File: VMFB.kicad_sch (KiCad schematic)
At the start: 109 parts, among them J1 Barrel_Jack_Switch, J10 Conn_01x03_Pin, J11 Conn_01x08_Pin, J12 Conn_01x04_Pin, J13 Conn_01x04_Pin, J14 Conn_01x04_Pin, J2 USB_B, J3 Screw_Terminal_01x02, J4 Screw_Terminal_01x03, J5 Conn_01x03_Pin, J6 Conn_01x04_Pin, J7 Conn_01x04_Pin, J8 Conn_01x04_Pin, J9 Conn_01x02_Pin, Q1 BC547, Q2 BC547, Q3 BC547, Q4 BD139, Q5 TIP41C, Q6 BC547, U1 LM358, U2 NE555P, U3 NE555P, U4 NE555P, U5 NE555P

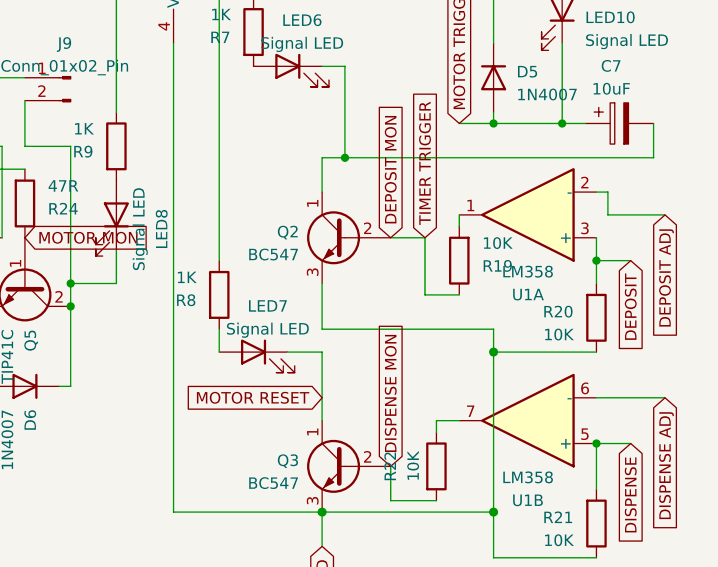
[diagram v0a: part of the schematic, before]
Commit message: Added 1uf cap on the dispense transistor base to prevent triggering on power-up.
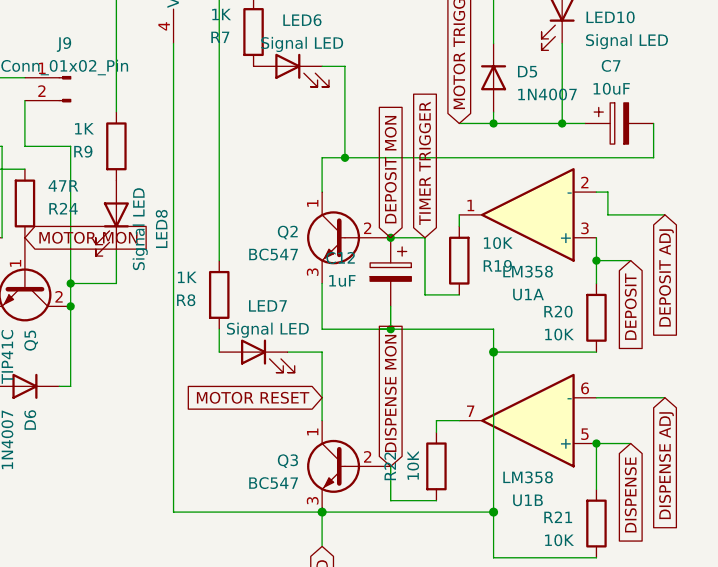
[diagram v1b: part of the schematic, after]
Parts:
- added C12: 1uF, Capacitor_THT:CP_Radial_D5.0mm_P2.00mm, symbol Device:C_Polarized
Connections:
- net DEPOSIT MON: now also C12.1
- net GND: now also C12.2
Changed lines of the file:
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@@
   (title_block
     (title "Vending Machine For Birds")
-    (date "2023-05-05")
-    (rev "A1.1")
+    (date "2023-06-23")
+    (rev "A1.2")
   )
   (junction (at 74.93 115.57) (diameter 0) (color 0 0 0 0)
@@
   (junction (at 57.15 95.25) (diameter 0) (color 221 119 0 1)
   )
+  (junction (at 251.46 54.61) (diameter 0) (color 0 0 0 0)
+  )
   (junction (at 110.49 27.94) (diameter 0) (color 194 0 0 1)
   )
@@
   )
   (junction (at 33.02 156.21) (diameter 1) (color 0 0 0 1)
+  )
+  (junction (at 251.46 64.77) (diameter 0) (color 0 0 0 0)
   )
   (junction (at 57.15 97.79) (diameter 1) (color 221 119 0 1)
@@
     (stroke (width 0) (type default) (color 153 12 207 1))
   )
+  (wire (pts (xy 251.46 64.77) (xy 262.89 64.77))
+    (stroke (width 0) (type default) (color 0 0 0 1))
+  )
   (wire (pts (xy 36.83 149.86) (xy 33.02 149.86))
     (stroke (width 0) (type default) (color 0 0 0 1))
@@
     (stroke (width 0) (type default))
   )
+  (wire (pts (xy 251.46 62.23) (xy 251.46 64.77))
+    (stroke (width 0) (type default))
+  )
   (wire (pts (xy 132.08 71.12) (xy 132.08 80.01))
     (stroke (width 0) (type default) (color 0 0 0 1))
@@
     (stroke (width 0) (type default))
   )
+  (wire (pts (xy 251.46 64.77) (xy 250.19 64.77))
+    (stroke (width 0) (type default))
+  )
   (wire (pts (xy 54.61 110.49) (xy 54.61 120.65))
     (stroke (width 0) (type default))
@@
     (stroke (width 0) (type default) (color 0 255 0 1))
   )
-  (wire (pts (xy 243.84 64.77) (xy 262.89 64.77))
+  (wire (pts (xy 243.84 64.77) (xy 251.46 64.77))
     (stroke (width 0) (type default) (color 0 0 0 1))
   )
@@
         )
       )
+    )
+  )
+  (symbol (lib_id "Device:C_Polarized") (at 251.46 58.42 0) (mirror y) (unit 1)
+    (in_bom yes) (on_board yes) (dnp no)
+    (property "Reference" "C12" (at 247.65 56.896 0)
+      (effects (font (size 1.27 1.27)) (justify left))
+    )
+    (property "Value" "1uF" (at 247.65 59.436 0)
+      (effects (font (size 1.27 1.27)) (justify left))
+    )
+    (property "Footprint" "Capacitor_THT:CP_Radial_D5.0mm_P2.00mm" (at 250.4948 62.23 0)
+      (effects (font (size 1.27 1.27)) hide)
+    )
+    (property "Datasheet" "~" (at 251.46 58.42 0)
+      (effects (font (size 1.27 1.27)) hide)
+    )
+    (pin "1")
+    (pin "2")
+    (instances
+      (project "VMFB"
+        (path "/840789ee-60d4-4003-8113-c1b030a45492"
+          (reference "C12") (unit 1)
+        )
+      )

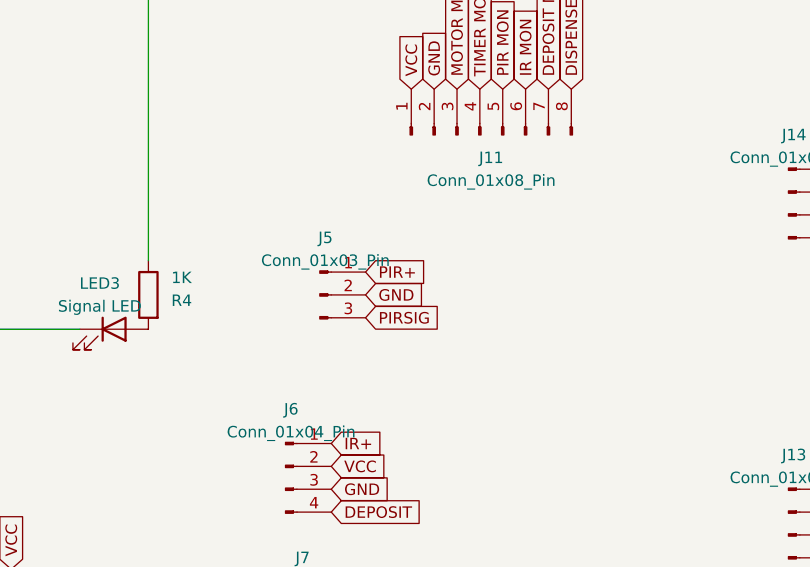
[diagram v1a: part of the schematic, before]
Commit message: Swapped PIR+ and GND to better accomodate common PIR pinouts.
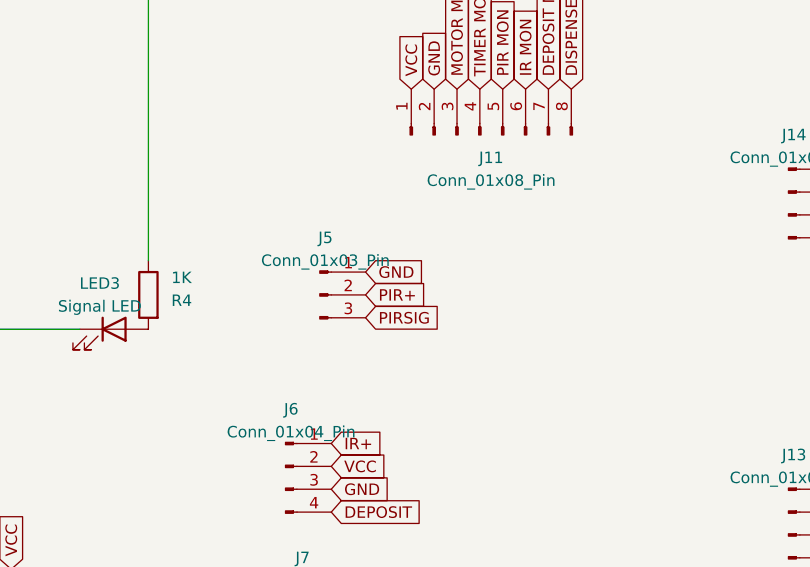
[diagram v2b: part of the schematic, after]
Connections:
- net GND: now also J5.1 (Pin_1); no longer J5.2 (Pin_2)
- net PIR+: now also J5.2 (Pin_2); no longer J5.1 (Pin_1)
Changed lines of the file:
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@@
     )
   )
-  (global_label "GND" (shape input) (at 149.86 123.19 0) (fields_autoplaced)
-    (effects (font (size 1.27 1.27)) (justify left))
-    (property "Intersheetrefs" "${INTERSHEET_REFS}" (at 156.6363 123.19 0) (show_name)
+  (global_label "GND" (shape input) (at 149.86 120.65 0) (fields_autoplaced)
+    (effects (font (size 1.27 1.27)) (justify left))
+    (property "Intersheetrefs" "${INTERSHEET_REFS}" (at 156.6363 120.65 0) (show_name)
       (effects (font (size 1.27 1.27)) (justify left) hide)
     )
@@
     )
   )
-  (global_label "PIR+" (shape input) (at 149.86 120.65 0) (fields_autoplaced)
-    (effects (font (size 1.27 1.27)) (justify left))
-    (property "Intersheetrefs" "${INTERSHEET_REFS}" (at 157.483 120.65 0) (show_name)
-      (effects (font (size 1.27 1.27)) (justify left) hide)
-    )
+  (global_label "PIR+" (shape input) (at 149.86 123.19 0) (fields_autoplaced)
+    (effects (font (size 1.27 1.27)) (justify left))
+    (property "Intersheetrefs" "${INTERSHEET_REFS}" (at 157.483 123.19 0) (show_name)
+      (effects (font (size 1.27 1.27)) (justify left) hide)
+    )

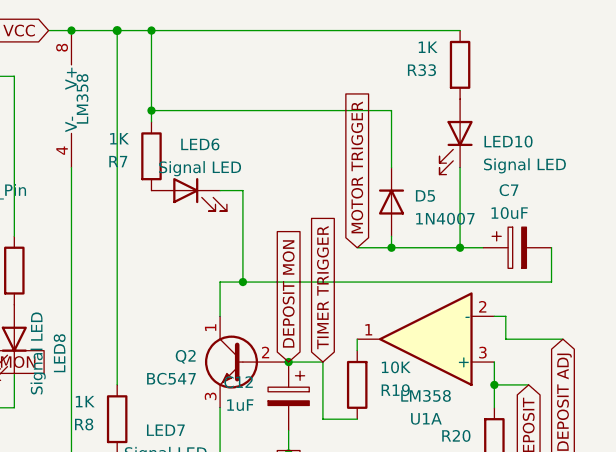
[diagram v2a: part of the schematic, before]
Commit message: Added 100K bleeder resistor across the pulse-shortening cap C7
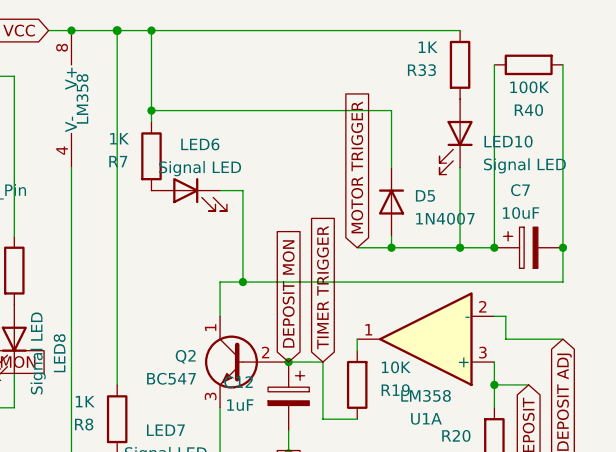
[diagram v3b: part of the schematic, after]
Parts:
- added R40: 100K, Resistor_THT:R_Axial_DIN0207_L6.3mm_D2.5mm_P2.54mm_Vertical, symbol Device:R
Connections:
- net MOTOR TRIGGER: now also R40.1
- net at C7.2, LED6.1 (K), Q2.1 (C): now also R40.2
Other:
- moved on the sheet: C7
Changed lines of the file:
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@@
   (junction (at 110.49 27.94) (diameter 0) (color 194 0 0 1)
   )
+  (junction (at 281.94 41.91) (diameter 0) (color 0 0 0 0)
+  )
   (junction (at 182.88 40.64) (diameter 1) (color 194 0 0 1)
   )
@@
   )
   (junction (at 69.85 130.81) (diameter 0) (color 0 0 0 1)
+  )
+  (junction (at 274.32 41.91) (diameter 0) (color 0 0 0 0)
   )
   (junction (at 262.89 85.09) (diameter 1) (color 0 0 0 1)
@@
     (stroke (width 0) (type default) (color 0 0 0 1))
   )
+  (wire (pts (xy 281.94 21.59) (xy 281.94 41.91))
+    (stroke (width 0) (type default))
+  )
   (wire (pts (xy 134.62 53.34) (xy 144.78 53.34))
     (stroke (width 0) (type default))
@@
     (stroke (width 0) (type default) (color 0 0 0 1))
   )
-  (wire (pts (xy 280.67 41.91) (xy 280.67 45.72))
+  (wire (pts (xy 281.94 41.91) (xy 281.94 45.72))
     (stroke (width 0) (type default))
   )
@@
     (stroke (width 0) (type default) (color 153 12 207 1))
   )
-  (wire (pts (xy 280.67 45.72) (xy 246.38 45.72))
+  (wire (pts (xy 281.94 45.72) (xy 246.38 45.72))
     (stroke (width 0) (type default))
   )
@@
     (stroke (width 0) (type default))
   )
+  (wire (pts (xy 274.32 21.59) (xy 274.32 41.91))
+    (stroke (width 0) (type default))
+  )
   (wire (pts (xy 110.49 27.94) (xy 110.49 30.48))
     (stroke (width 0) (type default) (color 194 0 0 1))
@@
     (stroke (width 0) (type default))
   )
-  (wire (pts (xy 270.51 41.91) (xy 273.05 41.91))
+  (wire (pts (xy 270.51 41.91) (xy 274.32 41.91))
     (stroke (width 0) (type default))
   )
@@
     )
   )
-  (symbol (lib_id "Device:C_Polarized") (at 276.86 41.91 90) (mirror x) (unit 1)
+  (symbol (lib_id "Device:C_Polarized") (at 278.13 41.91 90) (mirror x) (unit 1)
     (in_bom yes) (on_board yes) (dnp no) (fields_autoplaced)
-    (property "Reference" "C7" (at 275.971 35.56 90)
-      (effects (font (size 1.27 1.27)))
-    )
-    (property "Value" "10uF" (at 275.971 38.1 90)
-      (effects (font (size 1.27 1.27)))
-    )
-    (property "Footprint" "Capacitor_THT:CP_Radial_D5.0mm_P2.00mm" (at 280.67 42.8752 0)
-      (effects (font (size 1.27 1.27)) hide)
-    )
-    (property "Datasheet" "~" (at 276.86 41.91 0)
+    (property "Reference" "C7" (at 277.241 35.56 90)
+      (effects (font (size 1.27 1.27)))
+    )
+    (property "Value" "10uF" (at 277.241 38.1 90)
+      (effects (font (size 1.27 1.27)))
+    )
+    (property "Footprint" "Capacitor_THT:CP_Radial_D5.0mm_P2.00mm" (at 281.94 42.8752 0)
+      (effects (font (size 1.27 1.27)) hide)
+    )
+    (property "Datasheet" "~" (at 278.13 41.91 0)
       (effects (font (size 1.27 1.27)) hide)
     )
@@
         )
       )
+    )
+  )
+  (symbol (lib_id "Device:R") (at 278.13 21.59 90) (mirror x) (unit 1)
+    (in_bom yes) (on_board yes) (dnp no)
+    (property "Reference" "R40" (at 278.13 26.67 90)
+      (effects (font (size 1.27 1.27)))
+    )
+    (property "Value" "100K" (at 278.13 24.13 90)
+      (effects (font (size 1.27 1.27)))
+    )
+    (property "Footprint" "Resistor_THT:R_Axial_DIN0207_L6.3mm_D2.5mm_P2.54mm_Vertical" (at 278.13 19.812 90)
+      (effects (font (size 1.27 1.27)) hide)
+    )
+    (property "Datasheet" "~" (at 278.13 21.59 0)
+      (effects (font (size 1.27 1.27)) hide)
+    )
+    (pin "1")
+    (pin "2")
+    (instances
+      (project "VMFB"
+        (path "/840789ee-60d4-4003-8113-c1b030a45492"
+          (reference "R40") (unit 1)
+        )
+      )
